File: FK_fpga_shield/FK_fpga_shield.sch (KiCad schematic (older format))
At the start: 147 parts, among them J0 USB_B_Mini, J1 molex-51382-0400-microclasp, J10 molex-51382-0400-microclasp, J11 molex-51382-0400-microclasp, J12 molex-51382-0400-microclasp, J13 molex-51382-0400-microclasp, J14 molex-51382-0400-microclasp, J15 molex-51382-0400-microclasp, J16 molex-51382-0400-microclasp, J17 molex-51382-0400-microclasp, J18 molex-51382-0400-microclasp, J19 molex-51382-0400-microclasp, J2 molex-51382-0400-microclasp, J20 molex-51382-0400-microclasp, J21 molex-51382-0400-microclasp, J22 molex-51382-0400-microclasp, J23 molex-51382-0400-microclasp, J24 molex-51382-0400-microclasp, J25 molex-51382-0400-microclasp, J26 molex-51382-0400-microclasp, J27 molex-51382-0400-microclasp, J28 molex-51382-0400-microclasp, J29 molex-51382-0400-microclasp, J3 molex-51382-0400-microclasp, J30 molex-51382-0400-microclasp, J31 molex-51382-0400-microclasp, J32 molex-51382-0400-microclasp, J33 molex-51382-0400-microclasp, J34 molex-51382-0400-microclasp, J35 molex-51382-0400-microclasp, J36 Barrel_Jack_MountingPin, J4 molex-51382-0400-microclasp, J5 molex-51382-0400-microclasp, J6 molex-51382-0400-microclasp, J7 molex-51382-0400-microclasp, J8 molex-51382-0400-microclasp, J9 molex-51382-0400-microclasp, U1 FT232RL, U2 nvt2010pw, U3 nvt2010pw, U4 nvt2010pw, U5 nvt2010pw, U6 nvt2010pw, U7 nvt2010pw, U8 nvt2010pw, Y1 DNP_(12MHz)

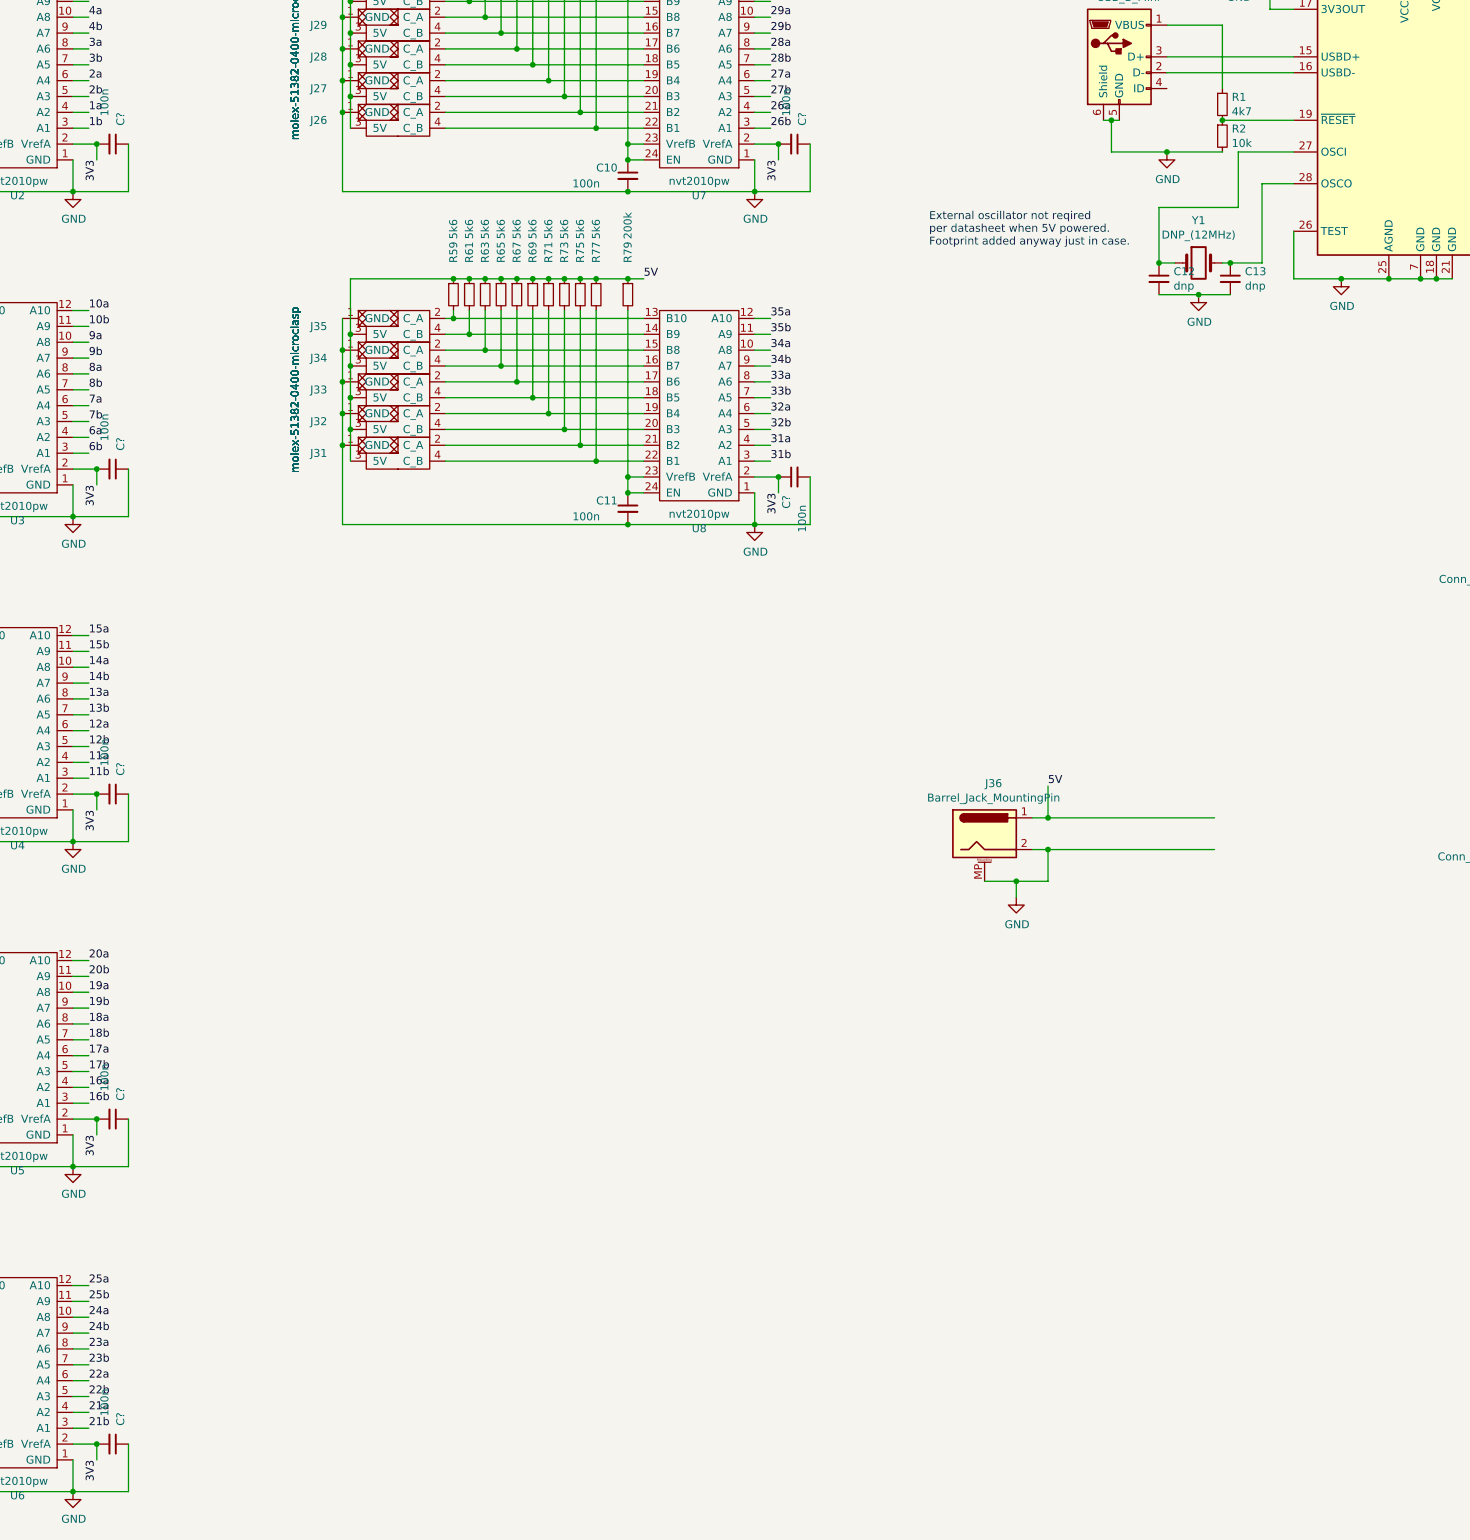
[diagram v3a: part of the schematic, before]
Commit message: redo 3v3 routing
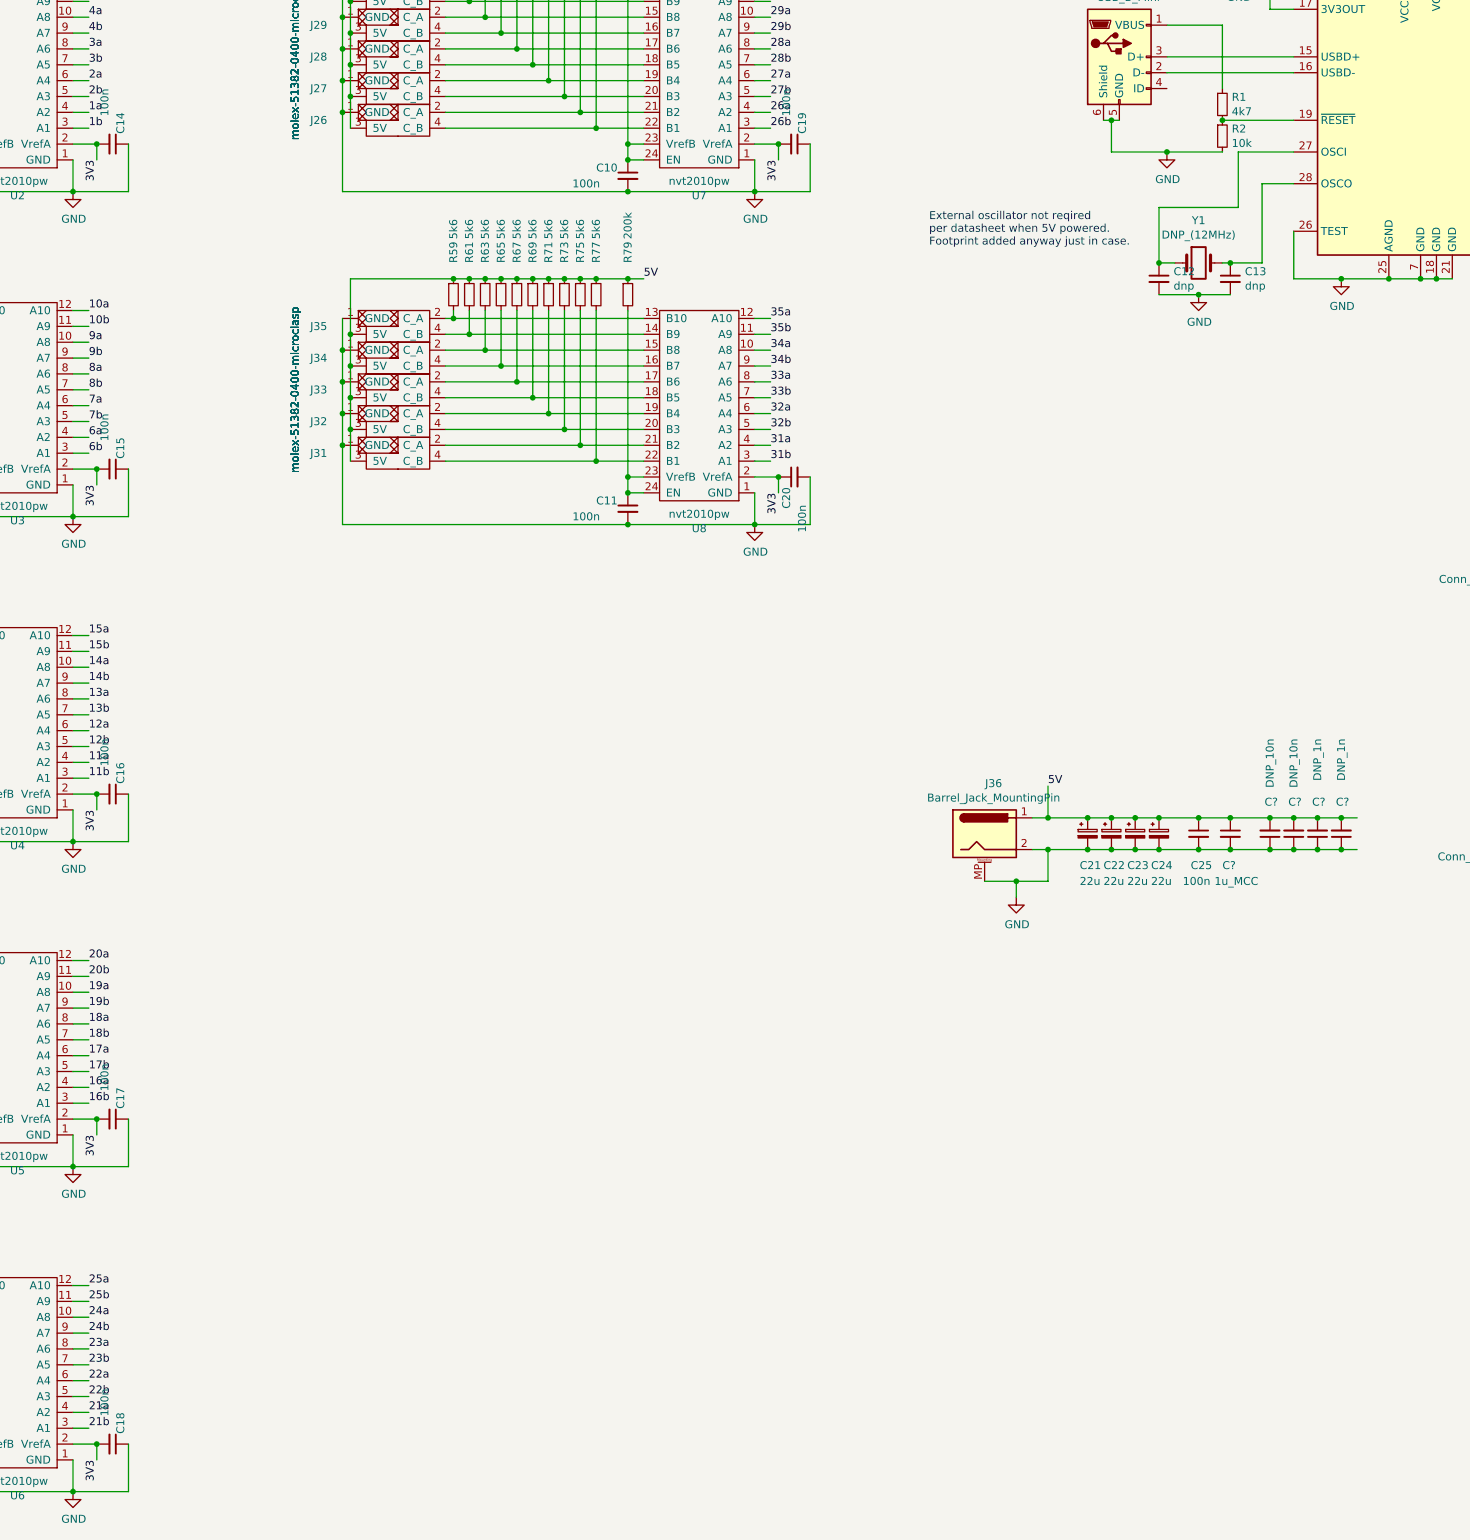
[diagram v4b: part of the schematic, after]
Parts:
- added C21, C22, C23, C24: 22u, Capacitor_THT:CP_Radial_D6.3mm_P2.50mm, symbol Device:CP_Small
- added C25: 100n, Capacitor_SMD:C_0805_2012Metric_Pad1.15x1.40mm_HandSolder, symbol Device:C_Small
- added C?: 1u_MCC, Capacitor_SMD:C_0805_2012Metric_Pad1.15x1.40mm_HandSolder, symbol Device:C_Small
- added C? (x2): DNP_10n, Capacitor_SMD:C_0805_2012Metric_Pad1.15x1.40mm_HandSolder, symbol Device:C_Small
- added C? (x2): DNP_1n, Capacitor_SMD:C_0805_2012Metric_Pad1.15x1.40mm_HandSolder, symbol Device:C_Small
- gave numbers to parts that had none: 7
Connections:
- net 5V: now also C21.1, C22.1, C23.1, C24.1, C25.1, C?.1, C?.2, C?.2, C?.2, C?.2
- net GND: now also C21.2, C22.2, C23.2, C24.2, C25.2, C?.1, C?.1, C?.1, C?.1, C?.2
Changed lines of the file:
@@
 	9500 6700 9600 6700
 Wire Wire Line
-	9600 6500 10650 6500
+	9600 6500 9850 6500
 Connection ~ 9600 6500
 Wire Wire Line
-	9600 6700 10650 6700
+	9600 6700 9850 6700
 Connection ~ 9600 6700
 $Comp
@@
 Connection ~ 9400 6900
 $Comp
-L Device:C_Small C?
+L Device:C_Small C20
 U 1 1 6051B8E6
 P 8000 4350
-F 0 "C?" H 7800 4400 50  0000 L CNN
+F 0 "C20" H 7800 4400 50  0000 L CNN
 F 1 "100n" H 7650 4300 50  0000 L CNN
 F 2 "Capacitor_SMD:C_0805_2012Metric_Pad1.15x1.40mm_HandSolder" H 8000 4350 50  0001 C CNN
@@
 	8100 4650 7750 4650
 $Comp
-L Device:C_Small C?
+L Device:C_Small C19
 U 1 1 60572E7D
 P 8000 2250
-F 0 "C?" H 7800 2300 50  0000 L CNN
+F 0 "C19" H 7800 2300 50  0000 L CNN
 F 1 "100n" H 7650 2200 50  0000 L CNN
 F 2 "Capacitor_SMD:C_0805_2012Metric_Pad1.15x1.40mm_HandSolder" H 8000 2250 50  0001 C CNN
@@
 	8100 2550 7750 2550
 $Comp
-L Device:C_Small C?
+L Device:C_Small C14
 U 1 1 605CB24D
 P 3700 2250
-F 0 "C?" H 3500 2300 50  0000 L CNN
+F 0 "C14" H 3500 2300 50  0000 L CNN
 F 1 "100n" H 3350 2200 50  0000 L CNN
 F 2 "Capacitor_SMD:C_0805_2012Metric_Pad1.15x1.40mm_HandSolder" H 3700 2250 50  0001 C CNN
@@
 	3800 2550 3450 2550
 $Comp
-L Device:C_Small C?
+L Device:C_Small C15
 U 1 1 6062316B
 P 3700 4300
-F 0 "C?" H 3500 4350 50  0000 L CNN
+F 0 "C15" H 3500 4350 50  0000 L CNN
 F 1 "100n" H 3350 4250 50  0000 L CNN
 F 2 "Capacitor_SMD:C_0805_2012Metric_Pad1.15x1.40mm_HandSolder" H 3700 4300 50  0001 C CNN
@@
 	3800 4600 3450 4600
 $Comp
-L Device:C_Small C?
+L Device:C_Small C16
 U 1 1 6067B91E
 P 3700 6350
-F 0 "C?" H 3500 6400 50  0000 L CNN
+F 0 "C16" H 3500 6400 50  0000 L CNN
 F 1 "100n" H 3350 6300 50  0000 L CNN
 F 2 "Capacitor_SMD:C_0805_2012Metric_Pad1.15x1.40mm_HandSolder" H 3700 6350 50  0001 C CNN
@@
 	3800 6650 3450 6650
 $Comp
-L Device:C_Small C?
+L Device:C_Small C17
 U 1 1 606D48EA
 P 3700 8400
-F 0 "C?" H 3500 8450 50  0000 L CNN
+F 0 "C17" H 3500 8450 50  0000 L CNN
 F 1 "100n" H 3350 8350 50  0000 L CNN
 F 2 "Capacitor_SMD:C_0805_2012Metric_Pad1.15x1.40mm_HandSolder" H 3700 8400 50  0001 C CNN
@@
 	3600 10450 3450 10450
 $Comp
-L Device:C_Small C?
+L Device:C_Small C18
 U 1 1 6072F97B
 P 3700 10450
-F 0 "C?" H 3500 10500 50  0000 L CNN
+F 0 "C18" H 3500 10500 50  0000 L CNN
 F 1 "100n" H 3350 10400 50  0000 L CNN
 F 2 "Capacitor_SMD:C_0805_2012Metric_Pad1.15x1.40mm_HandSolder" H 3700 10450 50  0001 C CNN
@@
 Wire Wire Line
 	3800 10750 3450 10750
+$Comp
+L Device:CP_Small C21
+U 1 1 607B4AE2
+P 9850 6600
+F 0 "C21" H 9800 6400 50  0000 L CNN
+F 1 "22u" H 9800 6300 50  0000 L CNN
+F 2 "Capacitor_THT:CP_Radial_D6.3mm_P2.50mm" H 9850 6600 50  0001 C CNN
+F 3 "~" H 9850 6600 50  0001 C CNN
+	1    9850 6600
+	1    0    0    -1
+$EndComp
+Connection ~ 9850 6500
+Wire Wire Line
+	9850 6500 10000 6500
+Connection ~ 9850 6700
+Wire Wire Line
+	9850 6700 10000 6700
+$Comp
+L Device:CP_Small C22
+U 1 1 607B61CF
+P 10000 6600
+F 0 "C22" H 9950 6400 50  0000 L CNN
+F 1 "22u" H 9950 6300 50  0000 L CNN
+F 2 "Capacitor_THT:CP_Radial_D6.3mm_P2.50mm" H 10000 6600 50  0001 C CNN
+F 3 "~" H 10000 6600 50  0001 C CNN
+	1    10000 6600
+	1    0    0    -1
+$EndComp
+Connection ~ 10000 6500
+Connection ~ 10000 6700
+$Comp
+L Device:C_Small C25
+U 1 1 607C709F
+P 10550 6600
+F 0 "C25" H 10500 6400 50  0000 L CNN
+F 1 "100n" H 10450 6300 50  0000 L CNN
+F 2 "Capacitor_SMD:C_0805_2012Metric_Pad1.15x1.40mm_HandSolder" H 10550 6600 50  0001 C CNN
+F 3 "~" H 10550 6600 50  0001 C CNN
+	1    10550 6600
+	1    0    0    -1
+$EndComp
+Wire Wire Line
+	10000 6500 10150 6500
+Wire Wire Line
+	10000 6700 10150 6700
+$Comp
+L Device:CP_Small C23
+U 1 1 607C8988
+P 10150 6600
+F 0 "C23" H 10100 6400 50  0000 L CNN
+F 1 "22u" H 10100 6300 50  0000 L CNN
+F 2 "Capacitor_THT:CP_Radial_D6.3mm_P2.50mm" H 10150 6600 50  0001 C CNN
+F 3 "~" H 10150 6600 50  0001 C CNN
+	1    10150 6600
+	1    0    0    -1
+$EndComp
+Connection ~ 10150 6500
+Wire Wire Line
+	10150 6500 10300 6500
+Connection ~ 10150 6700
+Wire Wire Line
+	10150 6700 10300 6700
+$Comp
+L Device:CP_Small C24
+U 1 1 607C8BED
+P 10300 6600
+F 0 "C24" H 10250 6400 50  0000 L CNN
+F 1 "22u" H 10250 6300 50  0000 L CNN
+F 2 "Capacitor_THT:CP_Radial_D6.3mm_P2.50mm" H 10300 6600 50  0001 C CNN
+F 3 "~" H 10300 6600 50  0001 C CNN
+	1    10300 6600
+	1    0    0    -1
+$EndComp
+Connection ~ 10300 6500
+Connection ~ 10300 6700
+Wire Wire Line
+	10300 6500 10550 6500
+Wire Wire Line
+	10300 6700 10550 6700
+Connection ~ 10550 6500
+Connection ~ 10550 6700
+$Comp
+L Device:C_Small C?
+U 1 1 607ED0DA
+P 10750 6600
+F 0 "C?" H 10700 6400 50  0000 L CNN
+F 1 "1u_MCC" H 10650 6300 50  0000 L CNN
+F 2 "Capacitor_SMD:C_0805_2012Metric_Pad1.15x1.40mm_HandSolder" H 10750 6600 50  0001 C CNN
+F 3 "~" H 10750 6600 50  0001 C CNN
+	1    10750 6600
+	1    0    0    -1
+$EndComp
+Wire Wire Line
+	10550 6500 10750 6500
+Wire Wire Line
+	10550 6700 10750 6700
+Connection ~ 10750 6500
+Connection ~ 10750 6700
+$Comp
+L Device:C_Small C?
+U 1 1 609644C2
+P 11000 6600
+F 0 "C?" H 10950 6400 50  0000 L CNN
+F 1 "DNP_10n" V 11000 6000 50  0000 L CNN
+F 2 "Capacitor_SMD:C_0805_2012Metric_Pad1.15x1.40mm_HandSolder" H 11000 6600 50  0001 C CNN
+F 3 "~" H 11000 6600 50  0001 C CNN
+	1    11000 6600
+	-1   0    0    1
+$EndComp
+Wire Wire Line
+	10750 6500 11000 6500
+Wire Wire Line
+	10750 6700 11000 6700
+Connection ~ 11000 6700
+Connection ~ 11000 6500
+Wire Wire Line
+	11000 6700 11150 6700
+Wire Wire Line
+	11000 6500 11150 6500
+$Comp
+L Device:C_Small C?
+U 1 1 609CA4EF
+P 11150 6600
+F 0 "C?" H 11100 6400 50  0000 L CNN
+F 1 "DNP_10n" V 11150 6000 50  0000 L CNN
+F 2 "Capacitor_SMD:C_0805_2012Metric_Pad1.15x1.40mm_HandSolder" H 11150 6600 50  0001 C CNN
+F 3 "~" H 11150 6600 50  0001 C CNN
+	1    11150 6600
+	-1   0    0    1
+$EndComp
+Connection ~ 11150 6700
+Wire Wire Line
+	11150 6700 11300 6700
+Connection ~ 11150 6500
+Wire Wire Line
+	11150 6500 11300 6500
+$Comp
+L Device:C_Small C?
+U 1 1 609CA843
+P 11300 6600
+F 0 "C?" H 11250 6400 50  0000 L CNN
+F 1 "DNP_1n" V 11300 6000 50  0000 L CNN
+F 2 "Capacitor_SMD:C_0805_2012Metric_Pad1.15x1.40mm_HandSolder" H 11300 6600 50  0001 C CNN
+F 3 "~" H 11300 6600 50  0001 C CNN
+	1    11300 6600
+	-1   0    0    1
+$EndComp
+Connection ~ 11300 6700
+Wire Wire Line
+	11300 6700 11450 6700
+Connection ~ 11300 6500
+Wire Wire Line
+	11300 6500 11450 6500
+$Comp
+L Device:C_Small C?
+U 1 1 609CAA01
+P 11450 6600
+F 0 "C?" H 11400 6400 50  0000 L CNN
+F 1 "DNP_1n" V 11450 6000 50  0000 L CNN
+F 2 "Capacitor_SMD:C_0805_2012Metric_Pad1.15x1.40mm_HandSolder" H 11450 6600 50  0001 C CNN
+F 3 "~" H 11450 6600 50  0001 C CNN
+	1    11450 6600
+	-1   0    0    1
+$EndComp
+Connection ~ 11450 6700
+Wire Wire Line
+	11450 6700 11550 6700
+Connection ~ 11450 6500
+Wire Wire Line
+	11450 6500 11550 6500
 $EndSCHEMATC
